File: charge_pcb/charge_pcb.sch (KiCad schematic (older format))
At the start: 29 parts, among them J1 PCB_1, J2 Battery, J3 Power Switch, J4 24V Out, J5 Motor_Left, J6 Motor_Cutter, J7 Motor_Right, Q1 BC547C, Q2 IRLML6344TRPBF, Q3 BC547C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

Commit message: Chargin Board changes
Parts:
- added D6: LED, LED_THT:LED_D1.8mm_W3.3mm_H2.4mm, symbol Device:LED
- added R9: 4.7kO, Resistor_THT:R_Axial_DIN0207_L6.3mm_D2.5mm_P7.62mm_Horizontal, symbol Device:R
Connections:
- net GND: now also D6.1 (K)
- net at D2.2 (K), Q2.3 (D), R1.1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: now also R9.1
- new net: D6.2 (A), R9.2
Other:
- moved on the sheet: D2
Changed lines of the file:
@@
 	2500 2250 2500 2400
 Wire Wire Line
-	1550 2250 1800 2250
+	1550 2250 1650 2250
 Wire Wire Line
 	2500 2700 2500 2900
 Wire Wire Line
 	2500 3500 2500 3700
-Wire Wire Line
-	2450 2900 2500 2900
 Connection ~ 2500 2900
 Wire Wire Line
@@
 L Lötpad_2,5mm:DIODE D2
 U 1 1 6071023D
-P 2000 2250
-F 0 "D2" H 2000 2442 40  0000 C CNN
-F 1 "SB1240" H 2000 2366 40  0000 C CNN
-F 2 "Diode_THT:D_DO-41_SOD81_P10.16mm_Horizontal" H 2000 2250 60  0001 C CNN
-F 3 "" H 2000 2250 60  0000 C CNN
-	1    2000 2250
+P 1850 2250
+F 0 "D2" H 1850 2442 40  0000 C CNN
+F 1 "SB1240" H 1850 2366 40  0000 C CNN
+F 2 "Diode_THT:D_DO-41_SOD81_P10.16mm_Horizontal" H 1850 2250 60  0001 C CNN
+F 3 "" H 1850 2250 60  0000 C CNN
+	1    1850 2250
 	1    0    0    -1
 $EndComp
@@
 	6500 2400 7050 2400
 Wire Wire Line
-	2200 2250 2500 2250
-Wire Wire Line
 	6500 2400 6500 3050
 Wire Wire Line
@@
 	1550 3700 650  3700
 Wire Wire Line
-	1550 3700 2500 3700
-Text GLabel 2450 2900 0    50   Output ~ 0
+	1550 3700 2000 3700
+Text GLabel 2250 3900 0    50   Output ~ 0
 pinChargeVoltage
 Wire Wire Line
@@
 Wire Wire Line
 	9700 3700 10100 3700
+$Comp
+L Device:R R9
+U 1 1 60730CD6
+P 2150 2550
+F 0 "R9" H 2220 2596 50  0000 L CNN
+F 1 "4.7kO" H 2220 2505 50  0000 L CNN
+F 2 "Resistor_THT:R_Axial_DIN0207_L6.3mm_D2.5mm_P7.62mm_Horizontal" V 2080 2550 50  0001 C CNN
+F 3 "~" H 2150 2550 50  0001 C CNN
+	1    2150 2550
+	1    0    0    -1
+$EndComp
+Wire Wire Line
+	2250 2900 2250 3900
+Wire Wire Line
+	2250 2900 2500 2900
+Connection ~ 1650 2250
+Wire Wire Line
+	1650 2250 1800 2250
+Wire Wire Line
+	2050 2250 2150 2250
+Wire Wire Line
+	2150 2400 2150 2250
+Connection ~ 2150 2250
+Wire Wire Line
+	2150 2250 2500 2250
+$Comp
+L Device:LED D6
+U 1 1 6073C265
+P 2000 2850
+F 0 "D6" V 2039 2732 50  0000 R CNN
+F 1 "LED" V 1948 2732 50  0000 R CNN
+F 2 "LED_THT:LED_D1.8mm_W3.3mm_H2.4mm" H 2000 2850 50  0001 C CNN
+F 3 "~" H 2000 2850 50  0001 C CNN
+	1    2000 2850
+	0    -1   -1   0
+$EndComp
+Wire Wire Line
+	2150 2700 2000 2700
+Wire Wire Line
+	2000 3000 2000 3700
+Connection ~ 2000 3700
+Wire Wire Line
+	2000 3700 2500 3700
 $EndSCHEMATC

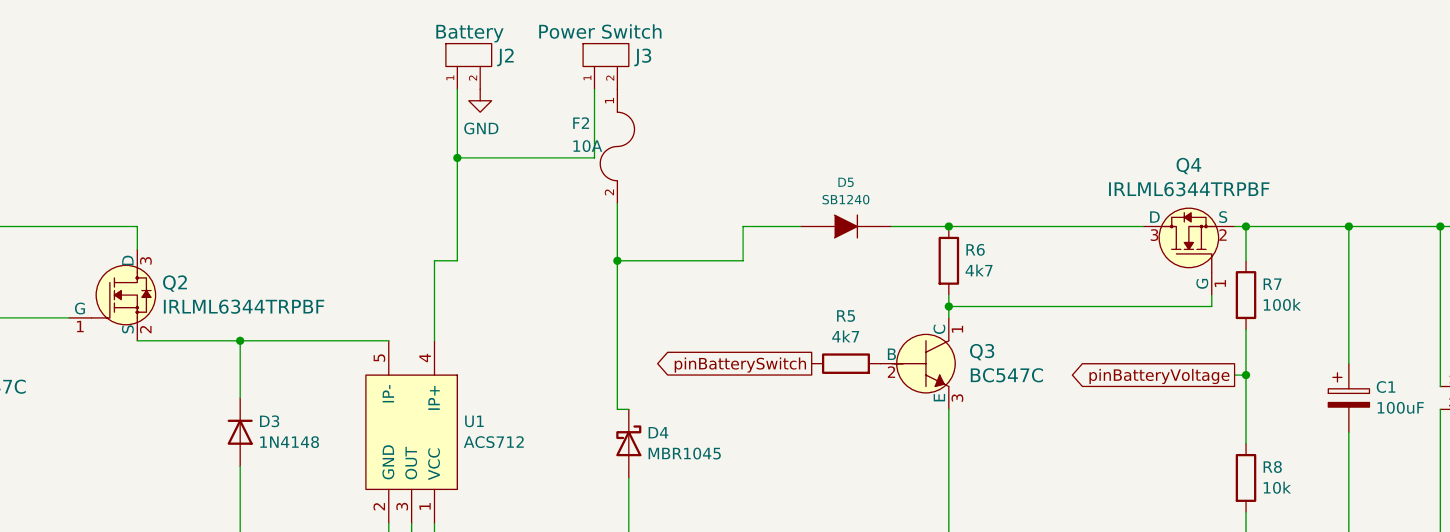
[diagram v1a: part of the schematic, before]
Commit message: Change Name of Mosfet
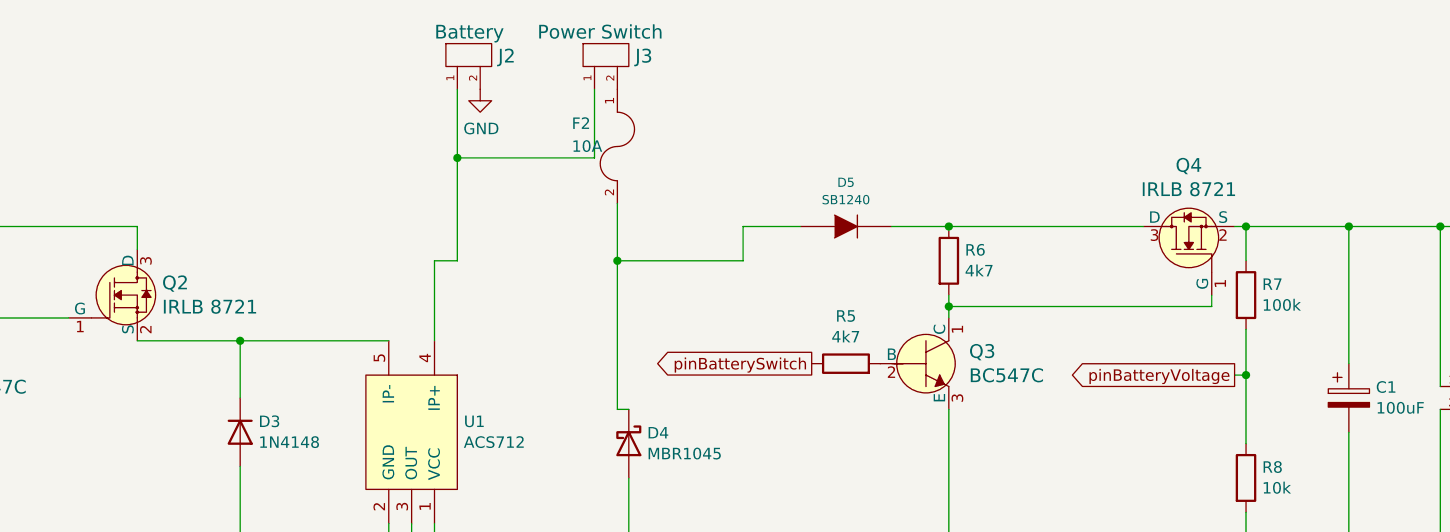
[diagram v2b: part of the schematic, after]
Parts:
- Q2, Q4: value IRLML6344TRPBF -> IRLB 8721
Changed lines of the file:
@@
 P 4400 2550
 F 0 "Q2" H 4508 2603 60  0000 L CNN
-F 1 "IRLML6344TRPBF" H 4508 2497 60  0000 L CNN
+F 1 "IRLB 8721" H 4508 2497 60  0000 L CNN
 F 2 "Package_TO_SOT_THT:SIPAK-1EP_Horizontal_TabDown" H 4600 2750 60  0001 L CNN
 F 3 "https://www.infineon.com/dgdl/irlml6344pbf.pdf?fileId=5546d462533600a4015356689c44262c" H 4600 2850 60  0001 L CNN
@@
 P 9000 2250
 F 0 "Q4" V 9267 2250 60  0000 C CNN
-F 1 "IRLML6344TRPBF" V 9161 2250 60  0000 C CNN
+F 1 "IRLB 8721" V 9161 2250 60  0000 C CNN
 F 2 "Package_TO_SOT_THT:SIPAK-1EP_Horizontal_TabDown" H 9200 2450 60  0001 L CNN
 F 3 "https://www.infineon.com/dgdl/irlml6344pbf.pdf?fileId=5546d462533600a4015356689c44262c" H 9200 2550 60  0001 L CNN

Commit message: Add Gerber Files
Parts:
- added H1, H2, H3, H4: MountingHole_Pad, MountingHole:MountingHole_3.2mm_M3_DIN965_Pad_TopBottom, symbol Mechanical:MountingHole_Pad
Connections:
- net GND: now also H1.1, H2.1, H3.1, H4.1
- no-connect marks 1 -> 0
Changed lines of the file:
@@
 Text GLabel 5500 6050 1    50   Output ~ 0
 pinBatteryVoltage
-NoConn ~ 3750 5650
 Wire Wire Line
 	650  2250 1050 2250
@@
 Wire Wire Line
 	2000 3700 2500 3700
+$Comp
+L Mechanical:MountingHole_Pad H1
+U 1 1 6073B4AE
+P 2600 5200
+F 0 "H1" H 2700 5249 50  0000 L CNN
+F 1 "MountingHole_Pad" H 2700 5158 50  0000 L CNN
+F 2 "MountingHole:MountingHole_3.2mm_M3_DIN965_Pad_TopBottom" H 2600 5200 50  0001 C CNN
+F 3 "~" H 2600 5200 50  0001 C CNN
+	1    2600 5200
+	1    0    0    -1
+$EndComp
+$Comp
+L Mechanical:MountingHole_Pad H2
+U 1 1 6073E1F7
+P 2600 5700
+F 0 "H2" H 2700 5749 50  0000 L CNN
+F 1 "MountingHole_Pad" H 2700 5658 50  0000 L CNN
+F 2 "MountingHole:MountingHole_3.2mm_M3_DIN965_Pad_TopBottom" H 2600 5700 50  0001 C CNN
+F 3 "~" H 2600 5700 50  0001 C CNN
+	1    2600 5700
+	1    0    0    -1
+$EndComp
+$Comp
+L Mechanical:MountingHole_Pad H3
+U 1 1 6073E399
+P 2600 6200
+F 0 "H3" H 2700 6249 50  0000 L CNN
+F 1 "MountingHole_Pad" H 2700 6158 50  0000 L CNN
+F 2 "MountingHole:MountingHole_3.2mm_M3_DIN965_Pad_TopBottom" H 2600 6200 50  0001 C CNN
+F 3 "~" H 2600 6200 50  0001 C CNN
+	1    2600 6200
+	1    0    0    -1
+$EndComp
+$Comp
+L Mechanical:MountingHole_Pad H4
+U 1 1 6073E5C5
+P 2600 6650
+F 0 "H4" H 2700 6699 50  0000 L CNN
+F 1 "MountingHole_Pad" H 2700 6608 50  0000 L CNN
+F 2 "MountingHole:MountingHole_3.2mm_M3_DIN965_Pad_TopBottom" H 2600 6650 50  0001 C CNN
+F 3 "~" H 2600 6650 50  0001 C CNN
+	1    2600 6650
+	1    0    0    -1
+$EndComp
+$Comp
+L Lötpad_2,5mm:GND #PWR0101
+U 1 1 6073E8B8
+P 2600 5300
+F 0 "#PWR0101" H 2600 5050 60  0001 C CNN
+F 1 "GND" H 2605 5119 60  0000 C CNN
+F 2 "" H 2600 5300 60  0000 C CNN
+F 3 "" H 2600 5300 60  0000 C CNN
+	1    2600 5300
+	1    0    0    -1
+$EndComp
+$Comp
+L Lötpad_2,5mm:GND #PWR0102
+U 1 1 607463A7
+P 2600 5800
+F 0 "#PWR0102" H 2600 5550 60  0001 C CNN
+F 1 "GND" H 2605 5619 60  0000 C CNN
+F 2 "" H 2600 5800 60  0000 C CNN
+F 3 "" H 2600 5800 60  0000 C CNN
+	1    2600 5800
+	1    0    0    -1
+$EndComp
+$Comp
+L Lötpad_2,5mm:GND #PWR0103
+U 1 1 60746674
+P 2600 6300
+F 0 "#PWR0103" H 2600 6050 60  0001 C CNN
+F 1 "GND" H 2605 6119 60  0000 C CNN
+F 2 "" H 2600 6300 60  0000 C CNN
+F 3 "" H 2600 6300 60  0000 C CNN
+	1    2600 6300
+	1    0    0    -1
+$EndComp
+$Comp
+L Lötpad_2,5mm:GND #PWR0104
+U 1 1 60746896
+P 2600 6750
+F 0 "#PWR0104" H 2600 6500 60  0001 C CNN
+F 1 "GND" H 2605 6569 60  0000 C CNN
+F 2 "" H 2600 6750 60  0000 C CNN
+F 3 "" H 2600 6750 60  0000 C CNN
+	1    2600 6750
+	1    0    0    -1
+$EndComp
 $EndSCHEMATC
